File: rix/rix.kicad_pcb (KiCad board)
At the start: 2 copper layers, 58 x 28 mm, 17 parts, among them J1 Barrel_Jack_Switch, J2 Conn_01x02_Male, J3 Conn_01x01_Male, U1 74LS04, U2 L78L05_SOT89, Y1 Crystal, Y2 Crystal

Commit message: PCB improvements
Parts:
- added D1: LED, Diode_SMD:D_1206_3216Metric_Pad1.42x1.75mm_HandSolder, F.Cu at (86.4, 82.5)
- added R3: 220R, Resistor_SMD:R_0805_2012Metric_Pad1.20x1.40mm_HandSolder, F.Cu at (86.4, 86.4)
- C1: value C_Polarized -> 50v 10uF; footprint Capacitor_THT:CP_Radial_D8.0mm_P3.50mm -> Capacitor_THT:CP_Radial_D5.0mm_P2.00mm
- C2: value C_Polarized -> 50v 1uF; footprint Capacitor_THT:CP_Radial_D8.0mm_P3.80mm -> Capacitor_THT:CP_Radial_D5.0mm_P2.00mm
- C3: value C_Small -> 10nF; footprint Capacitor_SMD:C_1206_3216Metric_Pad1.33x1.80mm_HandSolder -> Capacitor_SMD:C_0805_2012Metric_Pad1.18x1.45mm_HandSolder
- J1: footprint Connector_BarrelJack:BarrelJack_Horizontal -> Connector_BarrelJack:BarrelJack_Kycon_KLDX-0202-xC_Horizontal
- J2: value Conn_01x02_Male -> Detection coil; footprint Connector_PinSocket_2.54mm:PinSocket_1x02_P2.54mm_Vertical -> Connector_PinHeader_2.54mm:PinHeader_1x02_P2.54mm_Vertical
- J3: value Conn_01x01_Male -> External antenna; footprint Connector_Pin:Pin_D1.4mm_L8.5mm_W2.8mm_FlatFork -> Connector_PinHeader_2.54mm:PinHeader_1x01_P2.54mm_Vertical
- R1: value R -> 1M; moved to B.Cu
- RV1: value R_Potentiometer -> 10K
- U1: footprint Package_SO:SO-14_3.9x8.65mm_P1.27mm -> Package_SO:SOIC-14_3.9x8.7mm_P1.27mm
- Y1, Y2: value Crystal -> 8.0 Mhz Crystal
- moved J2 17.5 mm to (98.7, 89.9)
- moved U2 11.5 mm to (96.5, 85.1)
- moved RV1 7.14 mm to (117.3, 81.1)
- moved C3 6.86 mm to (110.5, 78.7)
- moved U1 6.84 mm to (110.5, 78.7)
- moved Y2 6.55 mm to (102.5, 71.1), turned to 0 degrees
- moved C1 5.90 mm to (90.2, 88.9), turned to 0 degrees
- moved Y1 5.82 mm to (106.8, 86.4)
- moved REF** 4.65 mm to (133.3, 91.0)
- moved REF** 4.65 mm to (133.3, 67.0)
- moved C2 3.81 mm to (101.6, 78.7)
- moved J3 3.59 mm to (116.8, 71.1)
- moved R2 2.84 mm to (113.0, 73.7)
- moved R1 2.55 mm to (109.2, 83.8), turned to 0 degrees
- moved J1 1.43 mm to (96.5, 75.4)
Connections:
- J3 pad 1: Net-(U1-Pad10) -> Net-(J3-Pad1)
- R2 pad 1: Net-(U1-Pad13) -> Net-(R2-Pad1)
- R2 pad 2: Net-(U1-Pad12) -> Net-(R2-Pad2)
- U1 pad 10: Net-(U1-Pad10) -> Net-(R2-Pad2)
- U1 pad 11: Net-(U1-Pad12) -> Net-(R2-Pad1)
- U1 pad 13: Net-(U1-Pad13) -> IF
- U1 pad 4: Net-(U1-Pad4) -> IF
- U1 pad 5: Net-(U1-Pad4) -> IF
- U1 pad 8: Net-(U1-Pad8) -> Net-(J3-Pad1)
- U1 pad 9: Net-(RV1-Pad1) -> Net-(R2-Pad2)
- Y1 pad 2: Net-(U1-Pad8) -> Net-(RV1-Pad1)
- Y2 pad 1: Net-(U1-Pad13) -> Net-(U1-Pad12)
- Y2 pad 2: Net-(U1-Pad4) -> Net-(R2-Pad1)
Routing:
- net GND: track 75.5 -> 0.00 mm, vias 2 -> 0
- net Net-(C2-Pad1): track 29.0 -> 0.00 mm, vias 1 -> 0
- net Net-(U1-Pad8): track 26.7 -> 0.00 mm
- net Net-(C1-Pad1): track 18.6 -> 0.00 mm
- net Net-(R1-Pad2): track 16.9 -> 0.00 mm
- net Net-(R1-Pad1): track 13.0 -> 0.00 mm
- net Net-(RV1-Pad1): track 12.8 -> 0.00 mm
- net Net-(U1-Pad4): track 11.4 -> 0.00 mm
- net Net-(U1-Pad13): track 7.32 -> 0.00 mm
- net Net-(U1-Pad10): track 5.67 -> 0.00 mm
- net Net-(U1-Pad12): track 3.99 -> 0.00 mm
- net Net-(J2-Pad2): track 3.85 -> 0.00 mm
- net Net-(J2-Pad1): track 3.33 -> 0.00 mm
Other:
- board size 58 x 28 mm -> 54.2 x 28.7 mm
- board text added: "RIX Metal Detector Version: 0.1.0-OH Open hardware By Dionys R."

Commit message: Adding tracks
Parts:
- moved C1 1.33 mm to (91.1, 89.9), turned to 90 degrees
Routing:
- net (no net): track 0.00 -> 184.8 mm
- net GND: track 0.00 -> 67.3 mm, vias 0 -> 1
- net Net-(C2-Pad1): track 0.00 -> 35.0 mm, vias 0 -> 2
- net Net-(J2-Pad1): track 0.00 -> 18.0 mm
- net Net-(C1-Pad1): track 0.00 -> 17.7 mm
- net Net-(J2-Pad2): track 0.00 -> 15.6 mm
- net Net-(RV1-Pad1): track 0.00 -> 11.3 mm
- net Net-(U1-Pad12): track 0.00 -> 10.5 mm
- net Net-(R1-Pad2): track 0.00 -> 9.72 mm
- net Net-(R2-Pad1): track 0.00 -> 8.57 mm
- net Net-(R1-Pad1): track 0.00 -> 8.32 mm
- net IF: track 0.00 -> 7.62 mm
- net Net-(J3-Pad1): track 0.00 -> 6.63 mm
- net Net-(R2-Pad2): track 0.00 -> 4.29 mm
- net Net-(D1-Pad2): track 0.00 -> 4.01 mm

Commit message: Adding gerber files
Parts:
- removed REF** (x4): MountingHole_2.2mm_M2_DIN965_Pad, MountingHole:MountingHole_2.2mm_M2_DIN965_Pad
- added H1: MountingHole_Pad, MountingHole:MountingHole_2.2mm_M2_DIN965_Pad_TopBottom, F.Cu at (133.3, 67.0)
- added H2: MountingHole_Pad, MountingHole:MountingHole_2.2mm_M2_DIN965_Pad_TopBottom, F.Cu at (133.4, 90.9)
- added H3: MountingHole_Pad, MountingHole:MountingHole_2.2mm_M2_DIN965_Pad_TopBottom, F.Cu at (84.0, 67.1)
- added H4: MountingHole_Pad, MountingHole:MountingHole_2.2mm_M2_DIN965_Pad_TopBottom, F.Cu at (84.0, 90.9)
- moved RV1 1.66 mm to (117.8, 79.5)
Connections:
- RV1 pad 1: Net-(RV1-Pad1) -> Net-(R1-Pad2)
- RV1 pad 3: Net-(R1-Pad2) -> Net-(RV1-Pad3)
- RV1 pad MP: (no net) -> GND
- U1 pad 6: Net-(RV1-Pad1) -> Net-(RV1-Pad3)
- Y1 pad 2: Net-(RV1-Pad1) -> Net-(RV1-Pad3)
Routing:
- net GND: track 67.3 -> 275.6 mm, vias 1 -> 16
- net (no net): track 184.8 -> 0.00 mm
- net Net-(RV1-Pad1): track 11.3 -> 0.00 mm
- net Net-(RV1-Pad3): track 0.00 -> 10.6 mm
- net Net-(R1-Pad2): track 9.72 -> 10.8 mm
- added copper zone on B.Cu, net GND
- added copper zone on F.Cu, net GND

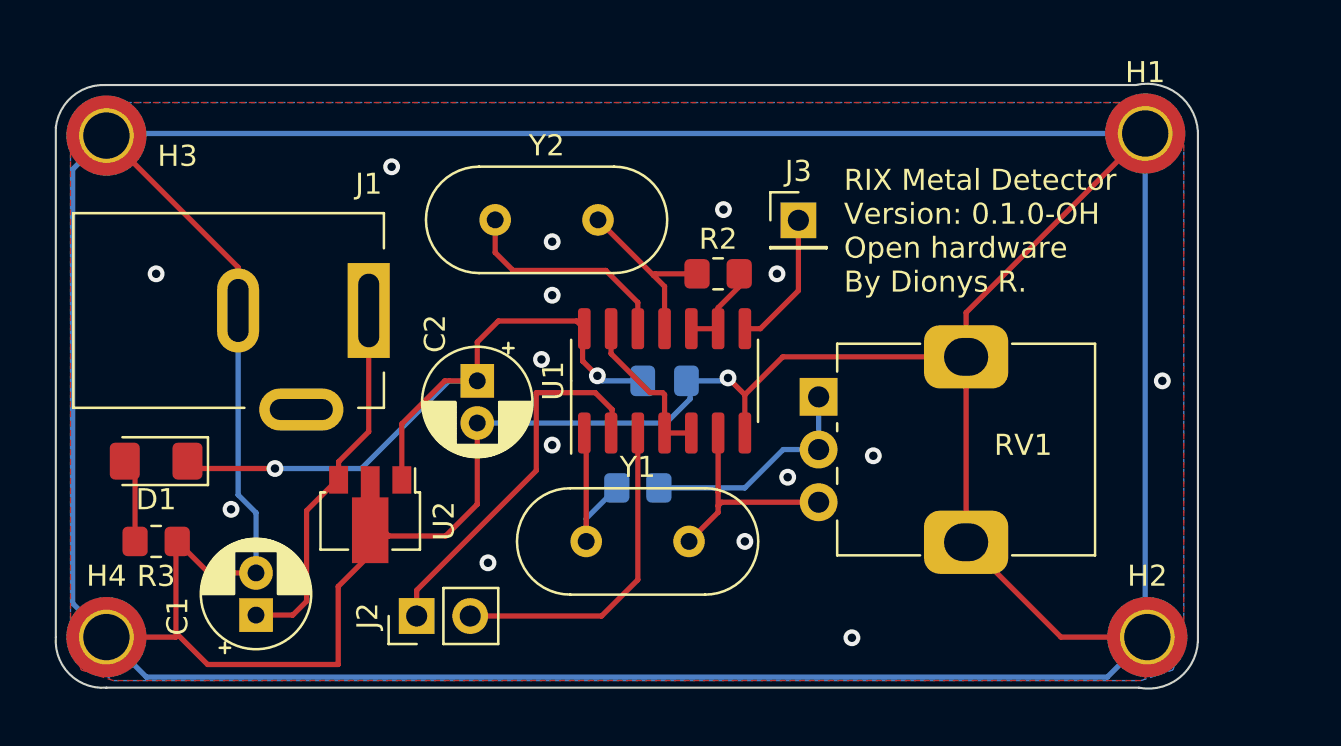
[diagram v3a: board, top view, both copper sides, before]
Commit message: Updating board constraits
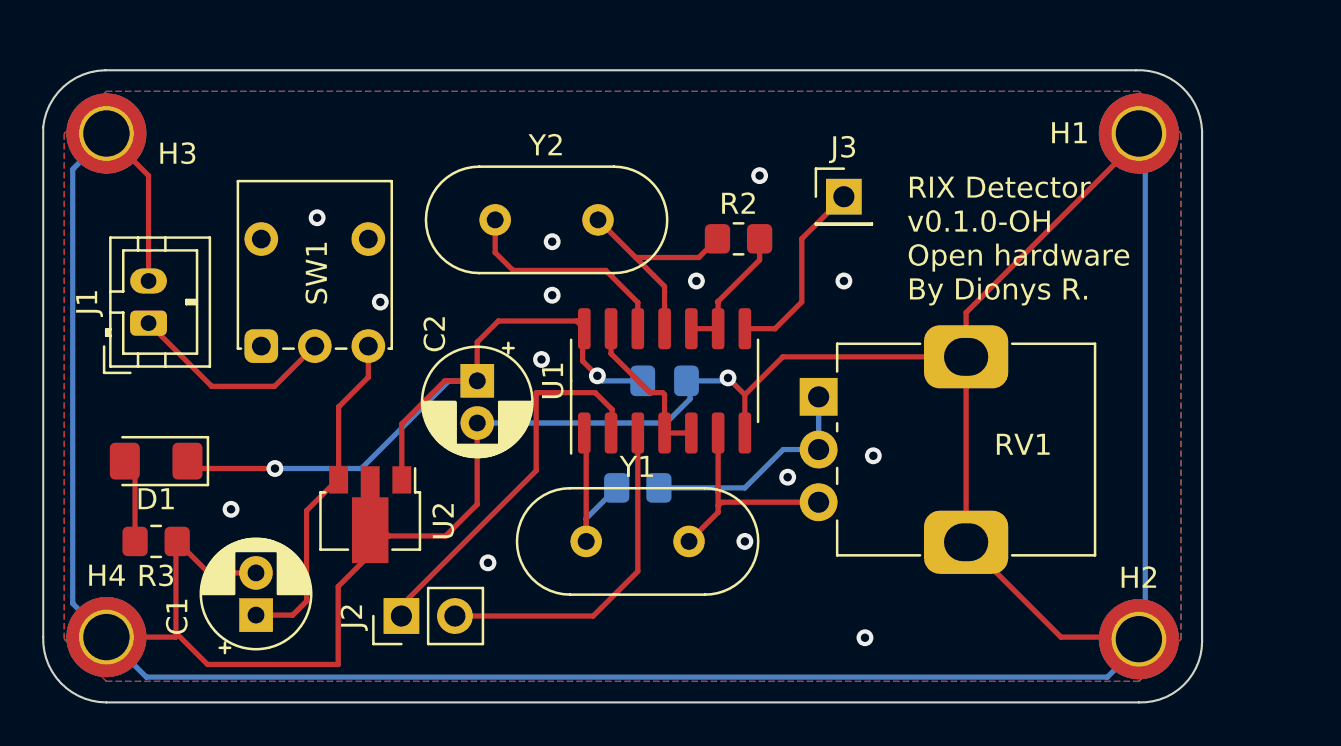
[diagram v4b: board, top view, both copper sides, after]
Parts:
- added SW1: On/Off SW, Button_Switch_THT:SW_Push_1P2T_Vertical_E-Switch_800UDP8P1A1M6, F.Cu at (91.3, 77.1)
- J1: value Barrel_Jack_Switch -> 9V BAT - +; footprint Connector_BarrelJack:BarrelJack_Kycon_KLDX-0202-xC_Horizontal -> Connector_JST:JST_PH_B2B-PH-K_1x02_P2.00mm_Vertical
- RV1: value 10K -> 10K tunnig POT
- moved J1 10.5 mm to (86.0, 76.0), turned to 90 degrees
- moved J3 2.43 mm to (119.0, 70.0)
- moved R2 1.92 mm to (114.0, 72.0)
- moved J2 0.72 mm to (98.0, 89.9)
- moved H2 0.41 mm to (133.0, 91.0)
- moved H1 0.30 mm to (133.0, 67.0)
- moved H3 0.10 mm to (84.0, 67.0)
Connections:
- J1 pad 1: Net-(C1-Pad1) -> Net-(J1-Pad1)
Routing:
- net GND: track 275.6 -> 210.5 mm, vias 16 -> 15
- net Net-(J1-Pad1): track 0.00 -> 9.92 mm
- net Net-(J3-Pad1): track 6.63 -> 9.05 mm
- net Net-(R2-Pad1): track 8.57 -> 10.7 mm
- net Net-(R2-Pad2): track 4.29 -> 6.38 mm
- net Net-(C1-Pad1): track 17.7 -> 16.0 mm
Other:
- board size 54.2 x 28.7 mm -> 55 x 30 mm
- board text added: "RIX Detector v0.1.0-OH Open hardware By Dionys R."
- board text removed: "RIX Metal Detector Version: 0.1.0-OH Open hardware By Dionys R."

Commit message: Update gerber files
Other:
- board text added: "RIX Detector v0.1.0-OSH Open Source hardware By Dionys R."
- board text removed: "RIX Detector v0.1.0-OH Open hardware By Dionys R."
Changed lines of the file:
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@@
   (gr_arc (start 81 66.7) (mid 81.959174 64.786412) (end 83.95 64) (layer "Edge.Cuts") (width 0.1))
   (gr_arc (start 84 94) (mid 81.843035 93.085773) (end 81 90.9) (layer "Edge.Cuts") (width 0.1))
-  (gr_text "RIX Detector\nv0.1.0-OH\nOpen hardware\nBy Dionys R.\n" (at 122 72) (layer "F.SilkS")
-    (effects (font (size 1 1) (thickness 0.125)) (justify left))
+  (gr_text "RIX Detector\nv0.1.0-OSH\nOpen Source hardware\nBy Dionys R.\n" (at 134 72) (layer "F.SilkS")
+    (effects (font (size 1 1) (thickness 0.125)) (justify right))
   )
   (segment (start 92.844888 89.855112) (end 93.5 89.2) (width 0.25) (layer "F.Cu") (net 1))
